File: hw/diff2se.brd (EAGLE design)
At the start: 33.6 x 20.9 mm, 24 parts, among them U1 MAX4478, X1 IN-, X2 IN+, X3 OUT

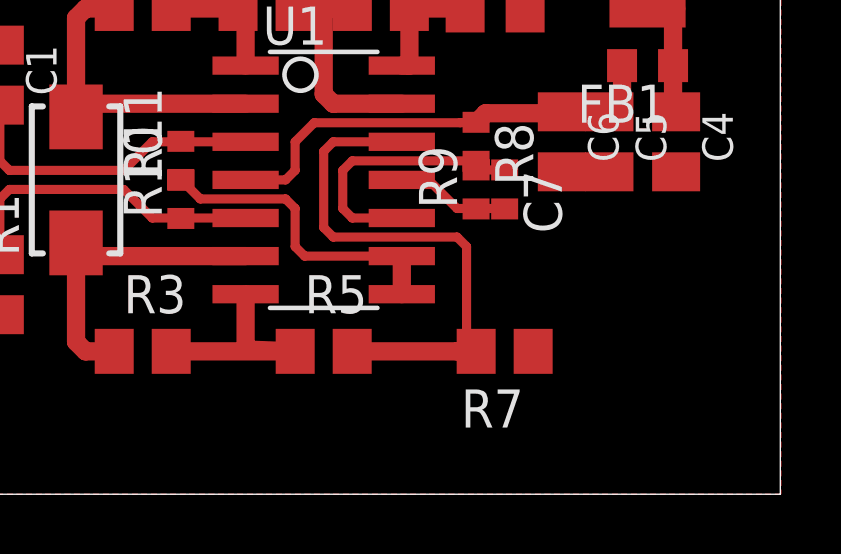
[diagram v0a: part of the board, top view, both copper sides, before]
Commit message: correct signal common to vref
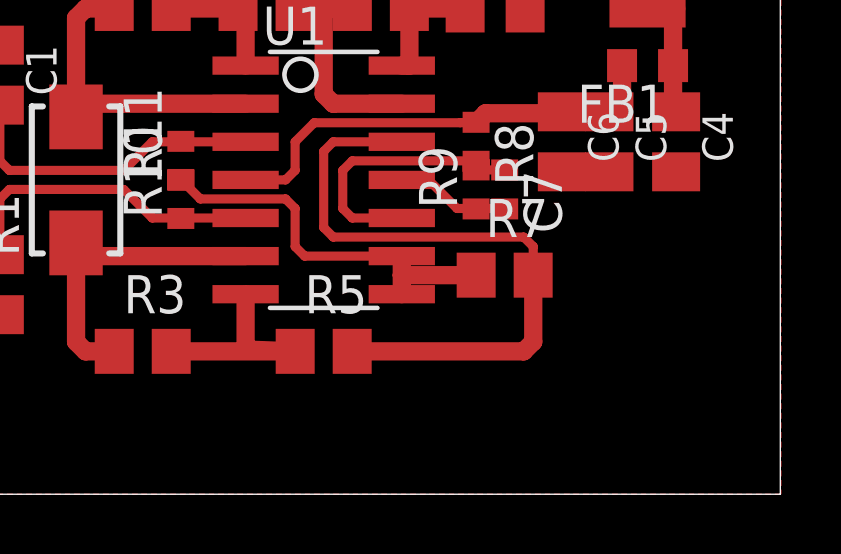
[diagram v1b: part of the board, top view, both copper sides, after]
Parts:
- moved R7 2.54 mm to (24.4, 26.4), turned to 0 degrees
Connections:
- net GND: no longer R7.1
- net VREF: now also R7.1
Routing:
- net N$10: track 18.1 -> 21.9 mm
- net VREF: track 10.4 -> 12.9 mm
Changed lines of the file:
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@@
 <element name="R5" library="rcl" package="R0805" value="" x="18.415" y="23.8125"/>
 <element name="R6" library="rcl" package="R0805" value="" x="20.32" y="35.2425"/>
-<element name="R7" library="rcl" package="R0805" value="" x="24.4475" y="23.8125" rot="R180"/>
+<element name="R7" library="rcl" package="R0805" value="" x="24.4475" y="26.3525"/>
 <element name="C3" library="rcl" package="C0805K" value="" x="24.13" y="35.2425"/>
 <element name="FB1" library="ferrite-bead" package="R0603" value="" x="29.21" y="33.3375" rot="R180"/>
@@
 <contactref element="X2" pad="G@3"/>
 <contactref element="X2" pad="G@4"/>
-<contactref element="R7" pad="1"/>
 <contactref element="X2" pad="G@1"/>
 <contactref element="X1" pad="G@1"/>
@@
 <contactref element="R5" pad="2"/>
 <contactref element="R7" pad="2"/>
-<wire x1="19.365" y1="23.8125" x2="22.86" y2="23.8125" width="0.6096" layer="1"/>
-<wire x1="22.86" y1="23.8125" x2="23.4975" y2="23.8125" width="0.6096" layer="1"/>
 <wire x1="21.0185" y1="30.7975" x2="18.7325" y2="30.7975" width="0.3048" layer="1"/>
 <wire x1="18.7325" y1="30.7975" x2="18.415" y2="30.48" width="0.3048" layer="1"/>
 <wire x1="18.415" y1="30.48" x2="18.415" y2="27.94" width="0.3048" layer="1"/>
 <wire x1="18.415" y1="27.94" x2="18.7325" y2="27.6225" width="0.3048" layer="1"/>
-<wire x1="18.7325" y1="27.6225" x2="22.86" y2="27.6225" width="0.3048" layer="1"/>
-<wire x1="22.86" y1="27.6225" x2="23.1775" y2="27.305" width="0.3048" layer="1"/>
-<wire x1="23.1775" y1="27.305" x2="23.1775" y2="24.13" width="0.3048" layer="1"/>
-<wire x1="23.1775" y1="24.13" x2="22.86" y2="23.8125" width="0.3048" layer="1"/>
+<wire x1="18.7325" y1="27.6225" x2="25.0825" y2="27.6225" width="0.3048" layer="1"/>
+<wire x1="25.0825" y1="27.6225" x2="25.4" y2="27.305" width="0.3048" layer="1"/>
+<wire x1="25.4" y1="27.305" x2="25.4" y2="26.355" width="0.3048" layer="1"/>
+<wire x1="25.4" y1="26.355" x2="25.3975" y2="26.3525" width="0.3048" layer="1"/>
+<wire x1="19.365" y1="23.8125" x2="25.0825" y2="23.8125" width="0.6096" layer="1"/>
+<wire x1="25.0825" y1="23.8125" x2="25.4" y2="24.13" width="0.6096" layer="1"/>
+<wire x1="25.4" y1="24.13" x2="25.4" y2="26.35" width="0.6096" layer="1"/>
+<wire x1="25.4" y1="26.35" x2="25.3975" y2="26.3525" width="0.6096" layer="1"/>
 </signal>
 <signal name="N$11">
@@
 <contactref element="R11" pad="1"/>
 <contactref element="R10" pad="2"/>
-<wire x1="21.0185" y1="25.7175" x2="21.0185" y2="26.9875" width="0.6096" layer="1"/>
+<wire x1="21.0185" y1="25.7175" x2="21.0185" y2="26.3525" width="0.6096" layer="1"/>
+<wire x1="21.0185" y1="26.3525" x2="21.0185" y2="26.9875" width="0.6096" layer="1"/>
 <wire x1="21.0185" y1="26.9875" x2="17.78" y2="26.9875" width="0.3048" layer="1"/>
 <wire x1="17.78" y1="26.9875" x2="17.4625" y2="27.305" width="0.3048" layer="1"/>
@@
 <wire x1="17.145" y1="28.8925" x2="14.3025" y2="28.8925" width="0.3048" layer="1"/>
 <wire x1="14.3025" y1="28.8925" x2="13.6525" y2="29.5425" width="0.3048" layer="1"/>
+<contactref element="R7" pad="1"/>
+<wire x1="23.4975" y1="26.3525" x2="21.0185" y2="26.3525" width="0.6096" layer="1"/>
 <wire x1="13.6525" y1="29.5425" x2="13.6525" y2="29.5125" width="0" layer="19" extent="1-1"/>
 </signal>
